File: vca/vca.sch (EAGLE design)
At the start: 83 parts, among them IC1 DG403DJD, IC2 OPA4130U, IC3 4001D, IC4 OPA2134D, IC5 OPA4130U, Q1 BC847ALT1SMD, Q2 BC857ALT1SMD, X1 2516-

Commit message: added a vca.  made changes to the filter components
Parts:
- removed A, ACVA, ASHAPE, AUV, D, DCVA, DSHAPE, OS: US-EVUF3J, dan:US-EVUF3J
- removed ACV, CVOUT, DCV, EOF, EOR, GATE: PJ301BM, dan:PJ301BM
- removed ADAR, CYCLE: (no value), dan:255SB
- removed C10, C11, C12, C13, C14, C5, C6, C7, C8, C9: 1u, dan:C-USC0603
- removed C2, C3, C4: (no value), dan:C-USC0603
- removed IC4: OPA2134D, dan:OPA2134D
- removed IC5: OPA4130U, dan:OPA4130U
- removed Q1: BC847ALT1SMD, dan:BC847ALT1SMD
- removed Q2: BC857ALT1SMD, dan:BC857ALT1SMD
- removed R23: 2.1k, dan:R-US_R0603
- removed R24, R26, R27, R33, R34, R35, R36, R37, R40, R41, R42, R43: 10k, dan:R-US_R0603
- removed R25, R28, R29, R30, R31, R32, R38, R39, R44, R45: 1k, dan:R-US_R0603
- added AMP, CVA: US-EVUF2J, dan:US-EVUF2J
- added CVIN, IN, OUT: PJ301BM, dan:PJ301BM
- added DCOS, RESP: 10k, dan:TRIM_US-RJ9W
- added U$1: SSM2212SOIC, dan:SSM2212SOIC
- added U$2: BCM847, dan:BCM847
- C1: value (none) -> 10n
- IC1: value DG403DJD -> OPA4130U; device dan:DG403DJD -> dan:OPA4130U
- IC2: value OPA4130U -> OPA134D; device dan:OPA4130U -> dan:OPA134D
- IC3: value 4001D -> OPA2134D; device dan:4001D -> dan:OPA2134D
- R1, R2: value 1meg -> 1k
- R11: value 1meg -> 10k
- R14, R4, R7: value 1k -> 10k
- R15: value 90 -> 10k
- R16: value 2.1k -> 10k
- R19, R20, R5, R9: value 10k -> 1k
- R21: value 90 -> 100k
- R22: value 2.1k -> 100k
- R6: value 10k -> 2Meg
- R8: value 10k -> 4.7k
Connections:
- removed net ASCV: IC5D.OUT, R19.2, R42.1
- removed net DSCV: IC5C.OUT, R26.2, R41.1
- removed net ENV: ASHAPE.E, AUV.E, C3.1, DSHAPE.E, IC1A.D1, IC2A.OUT, IC2B.+IN, IC2C.-IN, R33.2, R40.2, R43.2
- removed net IA: Q2.C, R3.2
- removed net ID: Q1.C, R4.1
- removed net N$29: D.A, R30.2
- removed net N$30: A.E, R32.1
- removed net N$31: D.S, R25.2
- removed net N$32: A.S, R18.2
- removed net N$33: IC5A.OUT, R34.1, R36.2
- removed net N$34: IC5A.-IN, R33.1, R34.2
- removed net N$35: CVOUT.P$3, R44.1
- removed net N$36: IC5B.OUT, R35.1, R44.2
- removed net N$37: OS.S, R37.2
- removed net N$38: ACV.P$3, ACVA.A
- removed net N$39: OS.A, R39.2
- removed net N$40: OS.E, R38.1
- removed net N$41: IC5D.-IN, R42.2, R43.1
- removed net N$42: IC5C.-IN, R40.1, R41.2
- removed net N$44: DCV.P$3, DCVA.E
- removed net N$45: ASHAPE.S, IC5D.+IN
- removed net N$46: DCVA.S, R27.2
- removed net N$47: EOR.P$3, R28.1
- removed net N$48: DSHAPE.S, IC5C.+IN
- removed net N$49: EOF.P$3, R45.1
- removed net N$50: ACVA.S, R20.2
- new net NEG8: IC1A.-IN, IC1A.OUT, IC1C.+IN, IC1D.+IN, U$2G$1.B
- net +12V: now also DCOS.S, IC1A.V+, IC2.V+, IC3P.V+, R19.1, R6.2, RESP.A; no longer C5.1, C6.1, C7.1, C8.1, C9.1, IC2A.V+, IC4P.V+, IC5A.V+, Q2.E, R13.2, R15.2, R22.2, R29.2, R32.2, R38.2, R5.2
- net -12V: now also IC1A.V-, IC2.V-, IC3P.V-, R8.2; no longer C10.1, C11.1, C12.1, C13.1, C14.1, IC2A.V-, IC4P.V-, IC5A.V-, R30.1, R31.1, R39.1, R9.1
- net GND: now also CVA.E, CVIN.P$1, CVIN.P$2, CVIN.P$4, IC1B.+IN, IN.P$1, IN.P$2, IN.P$4, OUT.P$1, OUT.P$2, OUT.P$4, R20.2, R5.2, R7.1, RESP.E, U$1G$2.B; no longer ACV.P$1, ACV.P$2, ACV.P$4, ACVA.E, ASHAPE.A, AUV.A, C10.2, C11.2, C12.2, C13.2, C14.2, C5.2, C6.2, C7.2, C8.2, C9.2, CVOUT.P$1, CVOUT.P$2, CVOUT.P$4, DCV.P$1, DCV.P$2, DCV.P$4, DCVA.A, DSHAPE.A, EOF.P$1, EOF.P$2, EOF.P$4, EOR.P$1, EOR.P$2, EOR.P$4, GATE.P$1, GATE.P$2, GATE.P$4, IC2A.+IN, IC4A.+IN, IC4B.+IN, IC5B.+IN, Q1.E, R1.1, R11.1, R12.1, R2.1, R21.1, R6.1, R8.2
- net N$1: now also R3.2, U$1G$1.E, U$1G$2.E; no longer IC3A.O, IC3B.I1
- net N$10: now also IC1A.+IN, R7.2, R8.1; no longer AUV.S, IC5A.+IN
- net N$11: now also IN.P$3, R4.2; no longer IC1A.IN, R10.2, R7.2
- net N$12: now also IC1D.-IN, R10.2, R11.1; no longer C2.2, IC2C.OUT
- net N$13: now also IC2.+IN, R14.2, R15.2; no longer IC2B.-IN, R5.1, R6.2
- net N$14: now also DCOS.E, R2.2; no longer C4.2, CYCLE.O, R10.1
- net N$15: now also DCOS.A, R1.2; no longer Q2.B, R14.2, R15.1, R16.1
- net N$16: now also IC2.-IN, R12.2, R13.1; no longer GATE.P$3, IC2D.-IN, R11.2
- net N$17: now also IC1B.OUT, R11.2, R16.1; no longer IC2D.+IN, R12.2, R13.1
- net N$18: now also IC2.OUT, OUT.P$3, R12.1; no longer ADAR.P, IC1B.IN
- net N$19: now also IC3B.-IN, IC3B.OUT, R17.2; no longer C1.2, CYCLE.P
- net N$2: now also R4.1, R5.1, U$1G$1.B; no longer ADAR.O, IC3A.I0, IC3B.O, R28.2
- net N$20: now also IC1B.-IN, R16.2, R17.1, R18.1; no longer ADAR.S, C4.1, IC2D.OUT
- net N$21: now also AMP.S, IC3B.+IN; no longer IC4A.OUT, R16.2, R17.1
- net N$22: now also AMP.A, R19.2; no longer IC4B.OUT, R23.2, R24.1
- net N$23: now also AMP.E; no longer IC4A.-IN, R17.2, R18.1, R19.1
- net N$24: now also IC3A.+IN, RESP.S; no longer IC4B.-IN, R24.2, R25.1, R26.1, R27.1
- net N$25: now also IC3A.-IN, R21.1, R22.2; no longer D.E, R29.1
- net N$26: now also CVA.A, CVIN.P$3; no longer Q1.B, R21.2, R22.1, R23.1
- net N$27: now also IC3A.OUT, R18.2, R21.2; no longer IC5B.-IN, R35.2, R36.1, R37.1
- net N$28: now also CVA.S, R22.1; no longer A.A, R31.2
- net N$3: now also R15.1, R2.1, U$1G$1.C; no longer C2.1, IC3A.I1, R1.2
- net N$4: now also R1.1, R13.2, U$1G$2.C; no longer C1.1, IC3B.I0, R2.2
- net N$5: now also C1.2, IC1C.OUT, U$2G$1.E, U$2G$2.E; no longer C3.2, IC1A.S1, IC1B.D2, IC1B.S1, IC2A.-IN
- net N$6: now also R3.1, U$2G$1.C; no longer IC1B.D1, R4.2
- net N$7: now also C1.1, IC1C.-IN, R6.1, U$2G$2.C; no longer IC1B.S2, R3.1
- net N$8: now also R9.1, U$2G$2.B; no longer IC2C.+IN, R8.1, R9.2
- net N$9: now also IC1D.OUT, R10.1, R9.2; no longer CYCLE.S, IC2B.OUT, R45.2, R7.1
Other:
- note removed: "Is this right?"
- note removed: "This is not confirmed."
- moved on the sheet: C1, R1, R10, R11, R12, R13, R14, R15, R16, R17, R18, R19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

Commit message: almost got the vca pcb done
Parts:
- added C2, C3, C4, C5, C6, C7: 10n, dan:C-USC0603
- added R23, R24: 10, dan:R-US_R0603
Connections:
- new net N$30: R23.2, X1-1.KL, X1-2.KL
- new net N$34: R24.2, X1-10.KL, X1-9.KL
- net +12V: now also C2.1, C3.1, C4.1, R24.1; no longer X1-10.KL, X1-9.KL
- net -12V: now also C5.1, C6.1, C7.1, R23.1; no longer X1-1.KL, X1-2.KL
- net GND: now also C2.2, C3.2, C4.2, C5.2, C6.2, C7.2, CVA.A; no longer CVA.E
- net N$26: now also CVA.E; no longer CVA.A
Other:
- moved on the sheet: CVA, X1-1, X1-10, X1-11, X1-12, X1-13, X1-14, X1-15, X1-16, X1-2, X1-3, X1-4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

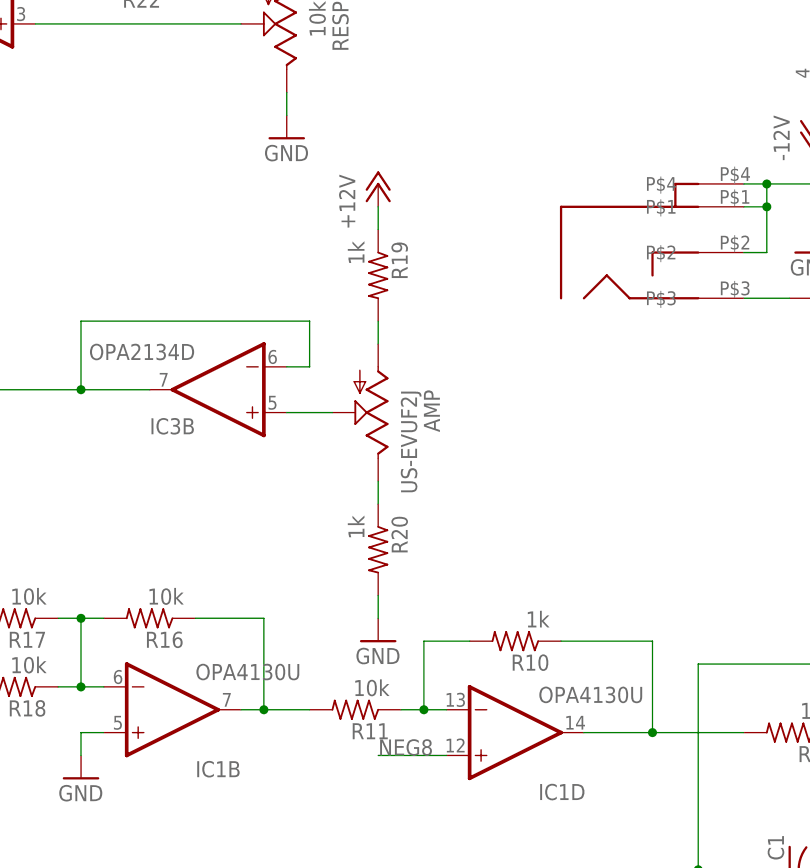
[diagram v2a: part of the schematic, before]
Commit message: fixed bugs in vca.  did more changing of vcf components.  need to route a trace in vcf
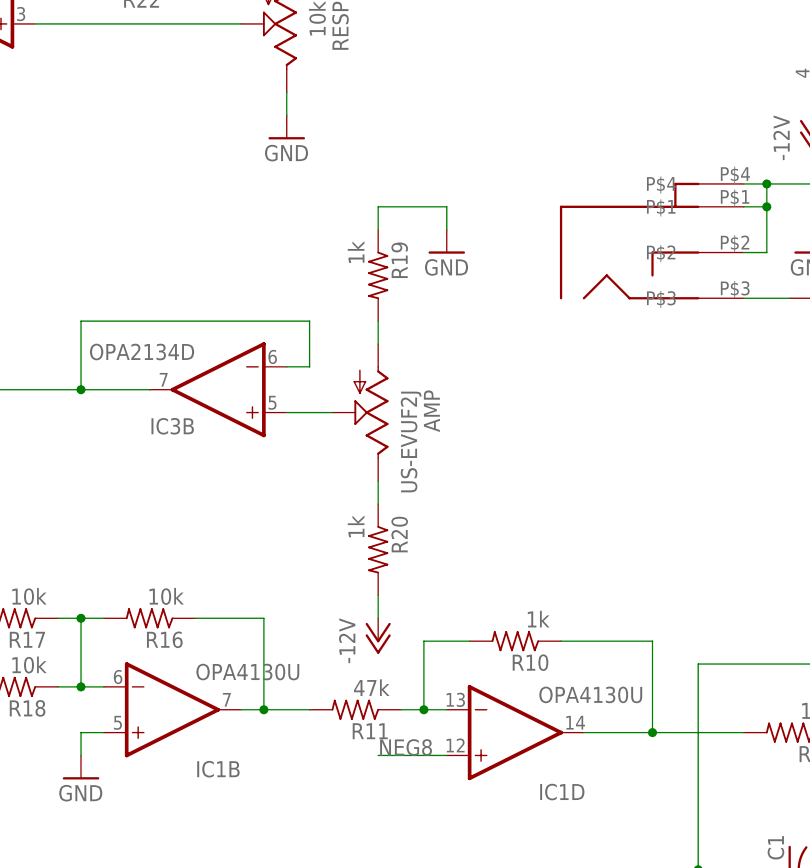
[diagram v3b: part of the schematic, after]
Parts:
- R11: value 10k -> 47k
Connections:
- net +12V: no longer R19.1
- net -12V: now also R20.2
- net GND: now also R19.1; no longer R20.2
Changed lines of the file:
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@@
 <part name="R9" library="dan" deviceset="R-US_" device="R0603" value="1k"/>
 <part name="R10" library="dan" deviceset="R-US_" device="R0603" value="1k"/>
-<part name="R11" library="dan" deviceset="R-US_" device="R0603" value="10k"/>
+<part name="R11" library="dan" deviceset="R-US_" device="R0603" value="47k"/>
 <part name="IN" library="dan" deviceset="PJ301BM" device=""/>
 <part name="GND3" library="dan" deviceset="GND" device=""/>
@@
 <part name="R19" library="dan" deviceset="R-US_" device="R0603" value="1k"/>
 <part name="R20" library="dan" deviceset="R-US_" device="R0603" value="1k"/>
-<part name="P+6" library="dan" deviceset="+12V" device=""/>
 <part name="GND8" library="dan" deviceset="GND" device=""/>
 <part name="RESP" library="dan" deviceset="TRIM_US-" device="RJ9W" value="10k"/>
@@
 <part name="R24" library="dan" deviceset="R-US_" device="R0603" value="10"/>
 <part name="GND13" library="dan" deviceset="GND" device=""/>
+<part name="P-7" library="dan" deviceset="-12V" device=""/>
 </parts>
 <sheets>
@@
 <instance part="R19" gate="G$1" x="-43.18" y="48.26" rot="R270"/>
 <instance part="R20" gate="G$1" x="-43.18" y="17.78" rot="R270"/>
-<instance part="P+6" gate="1" x="-43.18" y="58.42"/>
-<instance part="GND8" gate="1" x="-43.18" y="7.62"/>
+<instance part="GND8" gate="1" x="-35.56" y="50.8"/>
 <instance part="RESP" gate="G$1" x="-53.34" y="76.2" rot="R180"/>
 <instance part="P+7" gate="1" x="-53.34" y="88.9"/>
@@
 <instance part="R24" gate="G$1" x="-121.92" y="7.62" rot="R180"/>
 <instance part="GND13" gate="1" x="-114.3" y="63.5"/>
+<instance part="P-7" gate="1" x="-43.18" y="7.62"/>
 </instances>
 <busses>
@@
 <pinref part="IC1" gate="B" pin="+IN"/>
 <wire x1="-73.66" y1="-2.54" x2="-76.2" y2="-2.54" width="0.1524" layer="91"/>
-</segment>
-<segment>
-<pinref part="GND8" gate="1" pin="GND"/>
-<pinref part="R20" gate="G$1" pin="2"/>
-<wire x1="-43.18" y1="10.16" x2="-43.18" y2="12.7" width="0.1524" layer="91"/>
 </segment>
 <segment>
@@
 <wire x1="-114.3" y1="66.04" x2="-114.3" y2="68.58" width="0.1524" layer="91"/>
 </segment>
+<segment>
+<pinref part="R19" gate="G$1" pin="1"/>
+<wire x1="-43.18" y1="53.34" x2="-43.18" y2="55.88" width="0.1524" layer="91"/>
+<wire x1="-43.18" y1="55.88" x2="-35.56" y2="55.88" width="0.1524" layer="91"/>
+<pinref part="GND8" gate="1" pin="GND"/>
+<wire x1="-35.56" y1="55.88" x2="-35.56" y2="53.34" width="0.1524" layer="91"/>
+</segment>
 </net>
 <net name="N$6" class="0">
@@
 <pinref part="P+5" gate="1" pin="+12V"/>
 <wire x1="5.08" y1="83.82" x2="5.08" y2="86.36" width="0.1524" layer="91"/>
-</segment>
-<segment>
-<pinref part="R19" gate="G$1" pin="1"/>
-<pinref part="P+6" gate="1" pin="+12V"/>
-<wire x1="-43.18" y1="53.34" x2="-43.18" y2="55.88" width="0.1524" layer="91"/>
 </segment>
 <segment>
@@
 <junction x="-132.08" y="55.88"/>
 </segment>
-</net>
+<segment>
+<pinref part="P-7" gate="1" pin="-12V"/>
+<pinref part="R20" gate="G$1" pin="2"/>
+<wire x1="-43.18" y1="10.16" x2="-43.18" y2="12.7" width="0.1524" layer="91"/>
+</segment>
+</net>

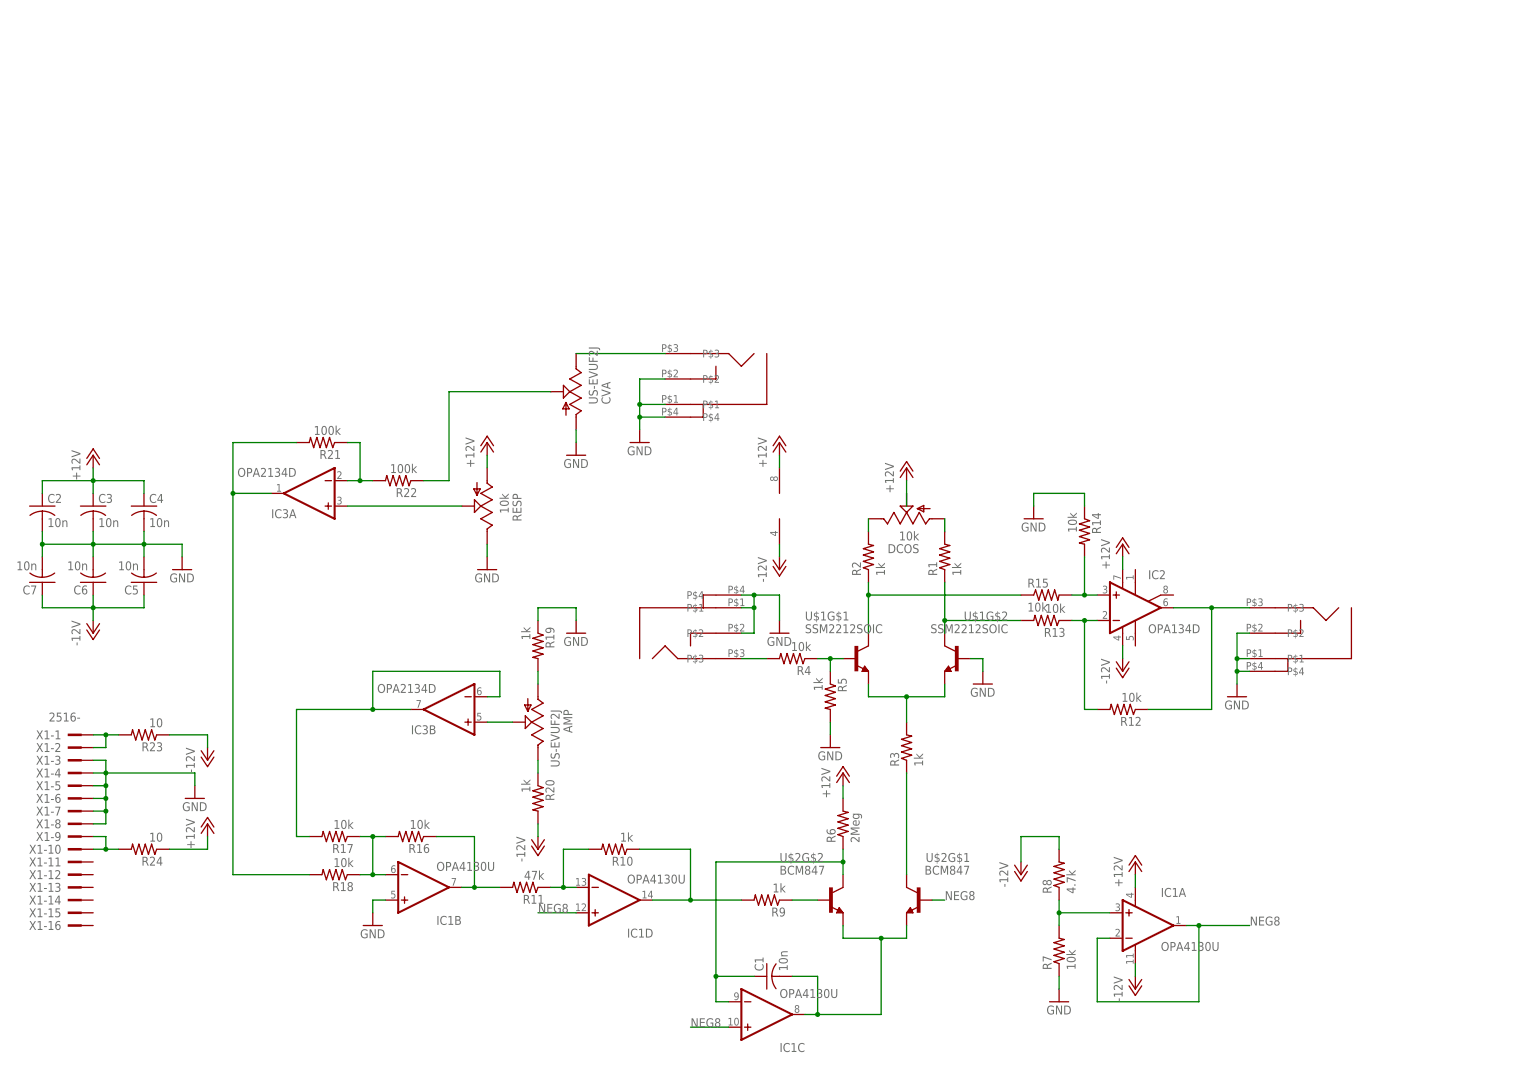
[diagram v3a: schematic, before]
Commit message: changed the vca to be a 2 board design with a mixer for the input.q
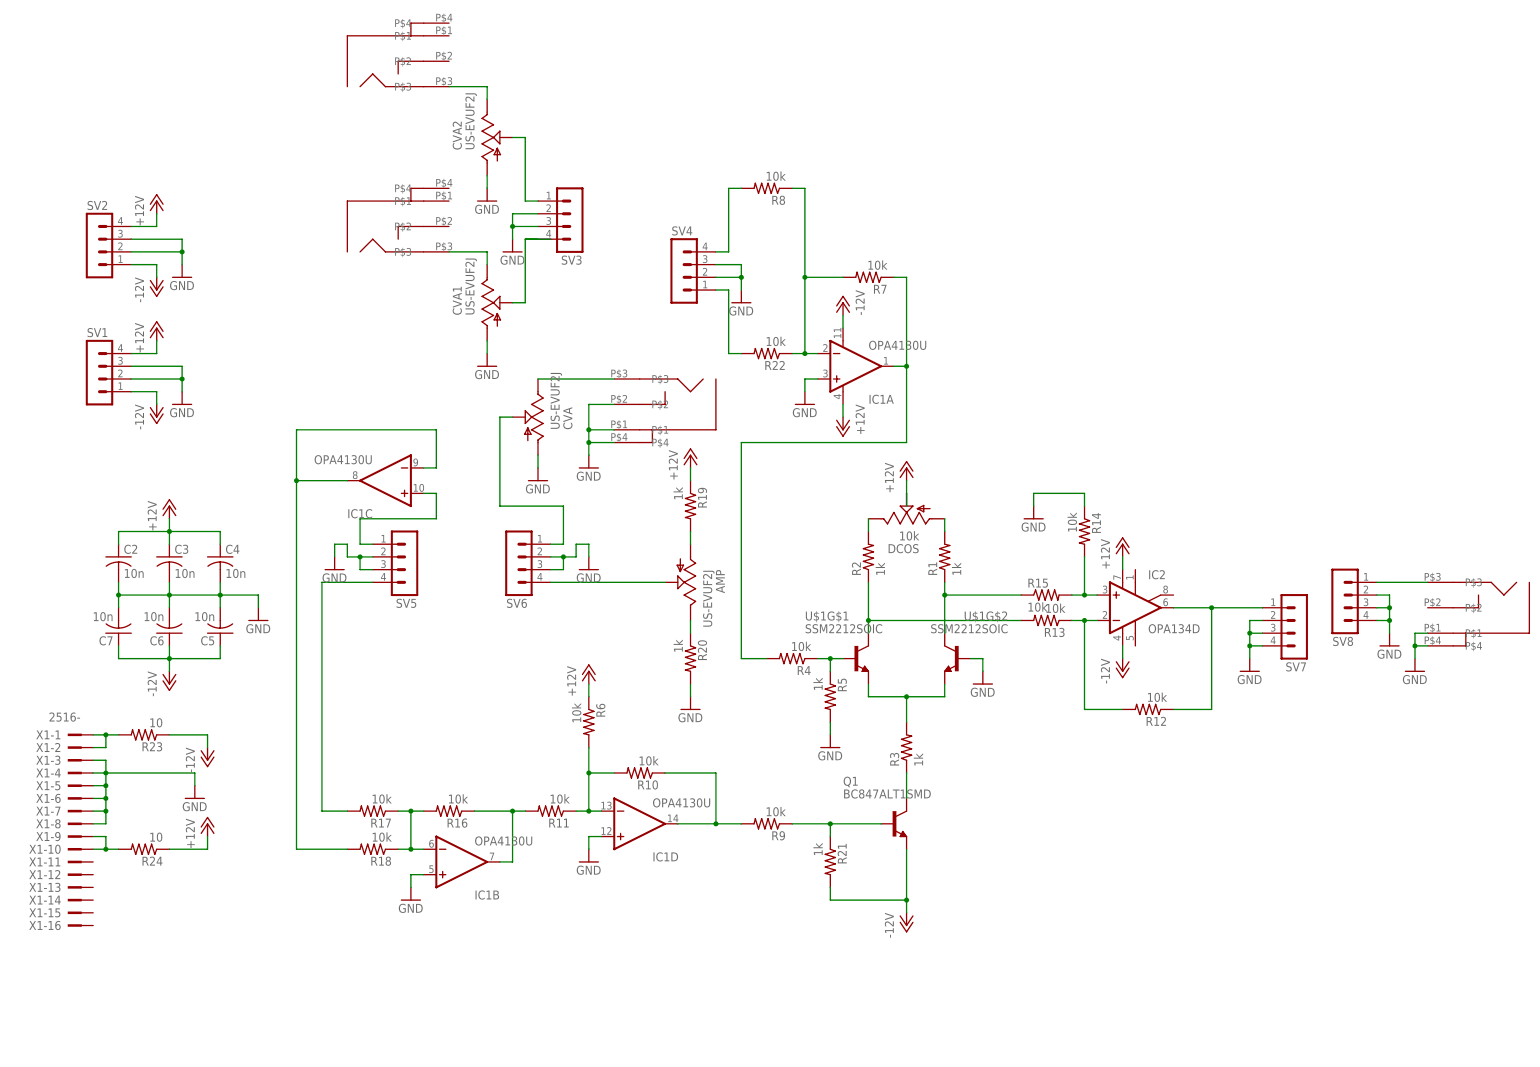
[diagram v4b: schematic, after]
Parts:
- removed C1: 10n, dan:C-USC0603
- removed IC3: OPA2134D, dan:OPA2134D
- removed IN: PJ301BM, dan:PJ301BM
- removed RESP: 10k, dan:TRIM_US-RJ9W
- removed U$2: BCM847, dan:BCM847
- added CVA1, CVA2: US-EVUF2J, dan:US-EVUF2J
- added IN1, IN2: PJ301BM, dan:PJ301BM
- added Q1: BC847ALT1SMD, dan:BC847ALT1SMD
- added SV1, SV2, SV3, SV4, SV5, SV6, SV7, SV8: (no value), dan:MA04-1
- R10, R9: value 1k -> 10k
- R11: value 47k -> 10k
- R21: value 100k -> 1k
- R22: value 100k -> 10k
- R6: value 2Meg -> 10k
- R8: value 4.7k -> 10k
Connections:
- removed net NEG8: IC1A.-IN, IC1A.OUT, IC1C.+IN, IC1D.+IN, U$2G$1.B
- new net N$29: R22.2, SV4.1
- new net N$31: CVA.S, SV6.1
- new net N$32: AMP.S, SV6.4
- new net N$33: IC1C.+IN, SV5.1
- net +12V: now also R19.1, R6.1, SV1.4, SV2.4; no longer IC3P.V+, R6.2, RESP.A
- net -12V: now also Q1.E, R21.2, SV1.1, SV2.1; no longer IC3P.V-, R20.2, R8.2
- net GND: now also CVA1.A, CVA2.A, IC1A.+IN, IC1D.+IN, R20.2, SV1.2, SV1.3, SV2.2, SV2.3, SV3.2, SV3.3, SV4.2, SV4.3, SV5.2, SV5.3, SV6.2, SV6.3, SV7.2, SV7.3, SV7.4, SV8.2, SV8.3, SV8.4; no longer IN.P$1, IN.P$2, IN.P$4, OUT.P$2, R19.1, R7.1, RESP.E
- net N$10: now also IC1A.-IN, R22.1; no longer IC1A.+IN
- net N$11: now also IC1A.OUT, R7.1; no longer IN.P$3
- net N$12: now also R6.2
- net N$18: now also SV7.1; no longer OUT.P$3
- net N$19: now also CVA2.S, SV3.1; no longer IC3B.-IN, IC3B.OUT, R17.2
- net N$21: now also CVA1.S, SV3.4; no longer AMP.S, IC3B.+IN
- net N$24: now also R17.2, SV5.4; no longer IC3A.+IN, RESP.S
- net N$25: now also CVA1.E, IN1.P$3; no longer IC3A.-IN, R21.1, R22.2
- net N$27: now also CVA2.E, IN2.P$3; no longer IC3A.OUT, R18.2, R21.2
- net N$28: now also R8.2, SV4.4; no longer CVA.S, R22.1
- net N$3: now also R13.2; no longer R15.1
- net N$4: now also R15.1; no longer R13.2
- net N$5: now also OUT.P$3, SV8.1; no longer C1.2, IC1C.OUT, U$2G$1.E, U$2G$2.E
- net N$6: now also IC1C.-IN, IC1C.OUT, R18.2; no longer R3.1, U$2G$1.C
- net N$7: now also Q1.C, R3.1; no longer C1.1, IC1C.-IN, R6.1, U$2G$2.C
- net N$8: now also Q1.B, R21.1; no longer U$2G$2.B
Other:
- moved on the sheet: AMP, C2, C3, C4, C5, C6, C7, CVA, IC1A, IC1B, IC1C, IC1D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
